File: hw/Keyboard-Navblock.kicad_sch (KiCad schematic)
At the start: 18 parts, among them X4000 Mounting-Hole-M3, X4001 Mounting-Hole-M3, X4002 Mounting-Hole-M3, X4003 Mounting-Hole-M3, X4004 Distance-Bolt_M3x5, X4005 Distance-Bolt_M3x5, X4006 Distance-Bolt_M3x5, X4007 Distance-Bolt_M3x5, X4008 Screw M3x10, X4009 Screw M3x10, X4010 Screw M3x10, X4011 Screw M3x10, X4012 Screw M3x10, X4013 Screw M3x10, X4014 Screw M3x10, X4015 Screw M3x10

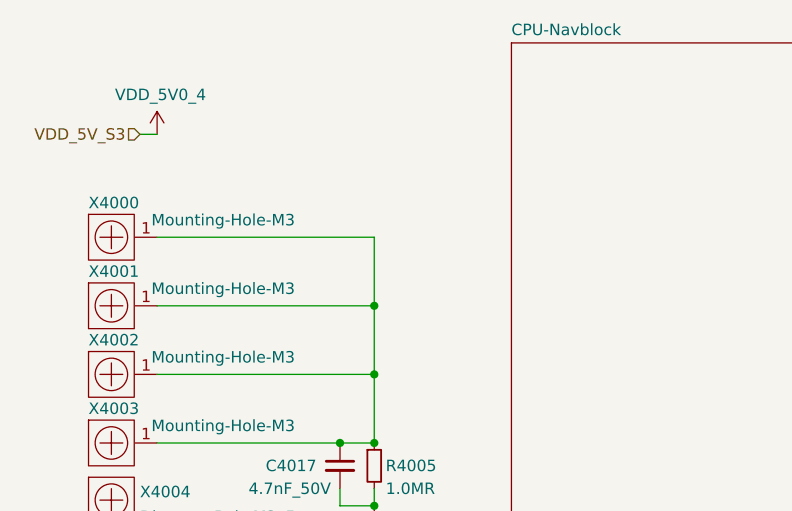
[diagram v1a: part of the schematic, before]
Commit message: Update schematic:
- Add ESD protection.
- Adjust distance bolts so they fit to the MX mounting plate.
- Make key layout symmetric.
- Add resistor to TX driver outputs.
- Use alternate IO functions on inter-board connectors.
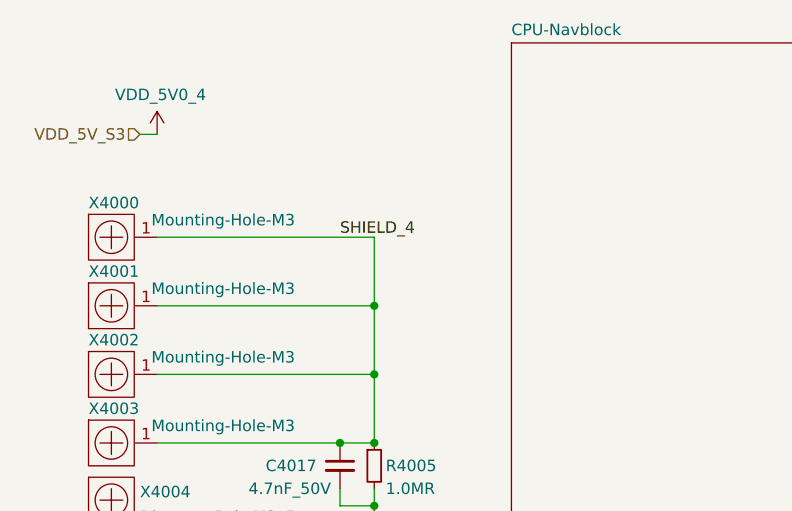
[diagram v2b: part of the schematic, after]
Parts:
- X4004, X4005, X4006, X4007: footprint Keyboard:DistanceBolt-M3x5 -> Keyboard:DistanceBolt-6x3.5; symbol Keyboard:Distance-Bolt_M3x5 -> Keyboard:Distance-Bolt_6x3.5
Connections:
- net SHIELD_4: now reaches C4017.1, R4005.1, X4000.1, X4001.1, X4002.1, X4003.1
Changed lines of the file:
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@@
+    (effects (font (size 1.27 1.27)) (justify left bottom))
+  )
+  (label "SHIELD_4" (at 57.15 46.99 0)
     (effects (font (size 1.27 1.27)) (justify left bottom))
   )
@@
     )
   )
-  (symbol (lib_id "Keyboard:Distance-Bolt_M3x5") (at 31.75 95.25 0) (unit 1)
+  (symbol (lib_id "Keyboard:Distance-Bolt_6x3.5") (at 31.75 95.25 0) (unit 1)
     (in_bom yes) (on_board yes) (fields_autoplaced)
     (property "Reference" "X4007" (id 0) (at 34.925 94.3415 0)
@@
       (effects (font (size 1.27 1.27)) (justify left))
     )
-    (property "Footprint" "Keyboard:DistanceBolt-M3x5" (id 2) (at 31.75 95.25 0)
+    (property "Footprint" "Keyboard:DistanceBolt-6x3.5" (id 2) (at 31.75 95.25 0)
       (effects (font (size 1.27 1.27)) hide)
     )
@@
     )
   )
-  (symbol (lib_id "Keyboard:Distance-Bolt_M3x5") (at 31.75 76.2 0) (unit 1)
+  (symbol (lib_id "Keyboard:Distance-Bolt_6x3.5") (at 31.75 76.2 0) (unit 1)
     (in_bom yes) (on_board yes) (fields_autoplaced)
     (property "Reference" "X4004" (id 0) (at 34.925 75.2915 0)
@@
       (effects (font (size 1.27 1.27)) (justify left))
     )
-    (property "Footprint" "Keyboard:DistanceBolt-M3x5" (id 2) (at 31.75 76.2 0)
+    (property "Footprint" "Keyboard:DistanceBolt-6x3.5" (id 2) (at 31.75 76.2 0)
       (effects (font (size 1.27 1.27)) hide)
     )
@@
     (pin "1")
   )
-  (symbol (lib_id "Keyboard:Distance-Bolt_M3x5") (at 31.75 88.9 0) (unit 1)
+  (symbol (lib_id "Keyboard:Distance-Bolt_6x3.5") (at 31.75 88.9 0) (unit 1)
     (in_bom yes) (on_board yes) (fields_autoplaced)
     (property "Reference" "X4006" (id 0) (at 34.925 87.9915 0)
@@
       (effects (font (size 1.27 1.27)) (justify left))
     )
-    (property "Footprint" "Keyboard:DistanceBolt-M3x5" (id 2) (at 31.75 88.9 0)
+    (property "Footprint" "Keyboard:DistanceBolt-6x3.5" (id 2) (at 31.75 88.9 0)
       (effects (font (size 1.27 1.27)) hide)
     )
@@
     )
   )
-  (symbol (lib_id "Keyboard:Distance-Bolt_M3x5") (at 31.75 82.55 0) (unit 1)
+  (symbol (lib_id "Keyboard:Distance-Bolt_6x3.5") (at 31.75 82.55 0) (unit 1)
     (in_bom yes) (on_board yes) (fields_autoplaced)
     (property "Reference" "X4005" (id 0) (at 34.925 81.6415 0)
@@
       (effects (font (size 1.27 1.27)) (justify left))
     )
-    (property "Footprint" "Keyboard:DistanceBolt-M3x5" (id 2) (at 31.75 82.55 0)
-      (effects (font (size 1.27 1.27)) hide)
-    )
+    (property "Footprint" "Keyboard:DistanceBolt-6x3.5" (id 2) (at 31.75 82.55 0)
+      (effects (font (size 1.27 1.27)) hide)
+    )
